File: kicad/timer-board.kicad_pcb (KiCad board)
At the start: 2 copper layers, 68.6 x 27.9 mm, 19 parts, among them J1 Conn_PWR, J2 Conn_Data, J3 JST Conn, SW1 SW_SPST, SW2 SW_SPDT, U1 NE555DR, U2 SN74HC00DR

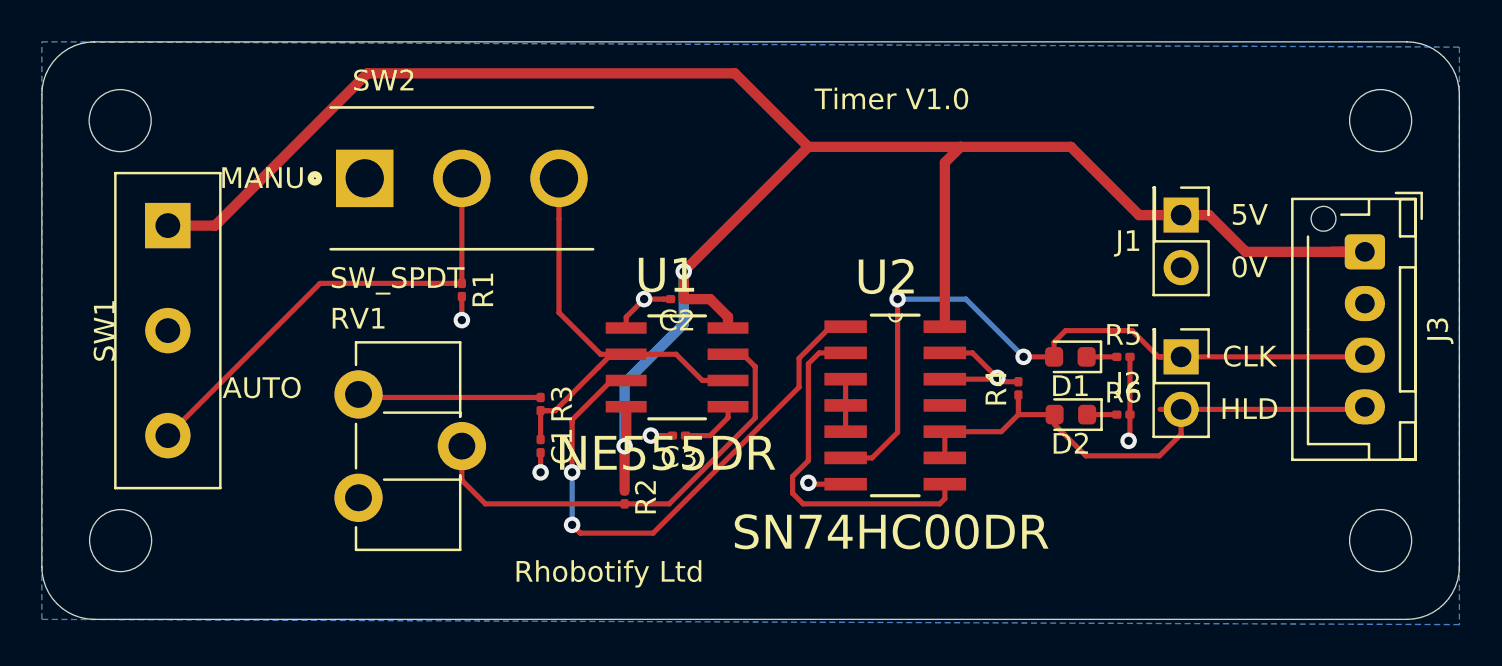
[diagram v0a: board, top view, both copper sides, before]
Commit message: Fix holes
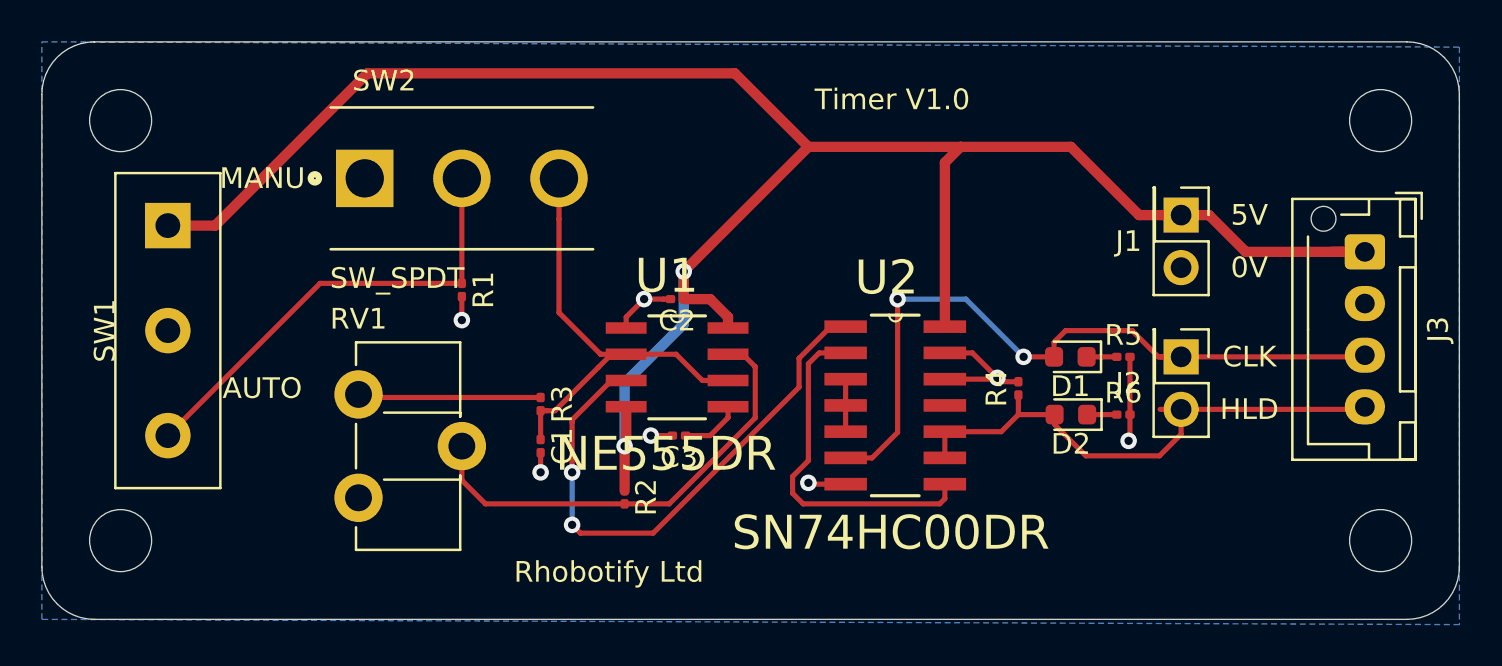
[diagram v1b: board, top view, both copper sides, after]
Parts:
- added REF**: MountingHole_3mm, MountingHole:MountingHole_3mm, F.Cu at (308.6, 105.4)
- added REF**: MountingHole_3mm, MountingHole:MountingHole_3mm, F.Cu at (308.6, 125.7)
- added REF**: MountingHole_3mm, MountingHole:MountingHole_3mm, F.Cu at (369.6, 125.7)
- added REF**: MountingHole_3mm, MountingHole:MountingHole_3mm, F.Cu at (369.6, 105.4)
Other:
- outline, holes or cut-outs redrawn
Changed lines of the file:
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@@
   (general
     (thickness 1.6)
-    (drawings 20)
+    (drawings 16)
     (tracks 140)
     (zones 0)
-    (modules 19)
+    (modules 23)
     (nets 15)
   )
@@
     (add_net "Net-(U2-Pad3)")
   )
+  (module MountingHole:MountingHole_3mm (layer F.Cu)
+    (at 308.61 105.41)
+    (descr "Mounting Hole 3mm, no annular")
+    (tags "mounting hole 3mm no annular")
+    (attr virtual)
+    (fp_text reference REF** (at 0 -4) (layer F.SilkS) hide
+      (effects (font (size 1 1) (thickness 0.15)))
+    )
+    (fp_text value MountingHole_3mm (at 0 4) (layer F.Fab)
+      (effects (font (size 1 1) (thickness 0.15)))
+    )
+    (fp_text user %R (at 0.3 0) (layer F.Fab)
+      (effects (font (size 1 1) (thickness 0.15)))
+    )
+    (fp_circle (center 0 0) (end 3 0) (layer Cmts.User) (width 0.15))
+    (fp_circle (center 0 0) (end 3.25 0) (layer F.CrtYd) (width 0.05))
+    (pad 1 np_thru_hole circle (at 0 0) (size 3 3) (drill 3) (layers *.Cu *.Mask))
+  )
+  (module MountingHole:MountingHole_3mm (layer F.Cu)
+    (at 308.61 125.73)
+    (descr "Mounting Hole 3mm, no annular")
+    (tags "mounting hole 3mm no annular")
+    (attr virtual)
+    (fp_text reference REF** (at 0 -4) (layer F.SilkS) hide
+      (effects (font (size 1 1) (thickness 0.15)))
+    )
+    (fp_text value MountingHole_3mm (at 0 4) (layer F.Fab)
+      (effects (font (size 1 1) (thickness 0.15)))
+    )
+    (fp_text user %R (at 0.3 0) (layer F.Fab)
+      (effects (font (size 1 1) (thickness 0.15)))
+    )
+    (fp_circle (center 0 0) (end 3 0) (layer Cmts.User) (width 0.15))
+    (fp_circle (center 0 0) (end 3.25 0) (layer F.CrtYd) (width 0.05))
+    (pad 1 np_thru_hole circle (at 0 0) (size 3 3) (drill 3) (layers *.Cu *.Mask))
+  )
+  (module MountingHole:MountingHole_3mm (layer F.Cu)
+    (at 369.57 125.73)
+    (descr "Mounting Hole 3mm, no annular")
+    (tags "mounting hole 3mm no annular")
+    (attr virtual)
+    (fp_text reference REF** (at 0 -4) (layer F.SilkS) hide
+      (effects (font (size 1 1) (thickness 0.15)))
+    )
+    (fp_text value MountingHole_3mm (at 0 4) (layer F.Fab)
+      (effects (font (size 1 1) (thickness 0.15)))
+    )
+    (fp_text user %R (at 0.3 0) (layer F.Fab)
+      (effects (font (size 1 1) (thickness 0.15)))
+    )
+    (fp_circle (center 0 0) (end 3 0) (layer Cmts.User) (width 0.15))
+    (fp_circle (center 0 0) (end 3.25 0) (layer F.CrtYd) (width 0.05))
+    (pad 1 np_thru_hole circle (at 0 0) (size 3 3) (drill 3) (layers *.Cu *.Mask))
+  )
+  (module MountingHole:MountingHole_3mm (layer F.Cu)
+    (at 369.57 105.41)
+    (descr "Mounting Hole 3mm, no annular")
+    (tags "mounting hole 3mm no annular")
+    (attr virtual)
+    (fp_text reference REF** (at 0 -4) (layer F.SilkS) hide
+      (effects (font (size 1 1) (thickness 0.15)))
+    )
+    (fp_text value MountingHole_3mm (at 0 4) (layer F.Fab)
+      (effects (font (size 1 1) (thickness 0.15)))
+    )
+    (fp_circle (center 0 0) (end 3.25 0) (layer F.CrtYd) (width 0.05))
+    (fp_circle (center 0 0) (end 3 0) (layer Cmts.User) (width 0.15))
+    (fp_text user %R (at 0.3 0) (layer F.Fab)
+      (effects (font (size 1 1) (thickness 0.15)))
+    )
+    (pad 1 np_thru_hole circle (at 0 0) (size 3 3) (drill 3) (layers *.Cu *.Mask))
+  )
   (module Connector_JST:JST_XH_B4B-XH-AM_1x04_P2.50mm_Vertical (layer F.Cu)
     (at 368.808 111.76 270)
@@
       (net 9 +5V))
   )
-  (gr_circle (center 369.57 105.41) (end 371.07 105.41) (layer Edge.Cuts) (width 0.05))
-  (gr_circle (center 369.57 125.73) (end 371.07 125.73) (layer Edge.Cuts) (width 0.05))
-  (gr_circle (center 308.61 125.73) (end 310.11 125.73) (layer Edge.Cuts) (width 0.05))
-  (gr_circle (center 308.588979 105.41) (end 310.088979 105.41) (layer Edge.Cuts) (width 0.05))
   (gr_arc (start 370.84 127) (end 370.84 129.54) (angle -90) (layer Edge.Cuts) (width 0.05))
   (gr_arc (start 307.34 127) (end 304.8 127) (angle -90) (layer Edge.Cuts) (width 0.05))

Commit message: Version 1.1
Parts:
- removed REF** (x4): MountingHole_3mm, MountingHole:MountingHole_3mm
- C1, C2, C3: footprint Capacitor_SMD:C_0201_0603Metric -> Capacitor_SMD:C_0603_1608Metric
- R1, R2, R3, R4, R5, R6: footprint Resistor_SMD:R_0201_0603Metric -> Resistor_SMD:R_0603_1608Metric
- moved R4 1.89 mm to (350.6, 119.6)
- moved D2 1.66 mm to (352.9, 119.5)
- moved D1 1.63 mm to (352.9, 116.8)
- moved C1 1.52 mm to (328.9, 122.7)
- moved R6 0.90 mm to (356.2, 119.5)
- moved R5 0.89 mm to (356.2, 116.8)
- moved R3 0.51 mm to (328.9, 119.6)
- moved R2 0.44 mm to (333.0, 123.2)
- moved C3 0.12 mm to (335.5, 120.7)
- moved C2 0.08 mm to (335.5, 114.0)
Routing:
- net GND: track 18.8 -> 23.7 mm, vias 7 -> 6
- net /Clk: track 36.5 -> 31.9 mm, vias 2 -> 0
- net /Hold: track 26.7 -> 23.4 mm
- net Net-(U1-Pad3): track 26.8 -> 29.6 mm
- net +5V: track 100.8 -> 98.6 mm
- net Net-(R2-Pad2): track 22.1 -> 23.9 mm
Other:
- board text added: "Timer V1.1"
- board text removed: "Timer V1.0"

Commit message: Update pot footprint
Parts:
- RV1: footprint Potentiometer_THT:Potentiometer_ACP_CA9-H5_Horizontal -> mine:6mm_trimmer
- moved RV1 1.45 mm to (318.8, 118.1)
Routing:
- net /Clk: track 31.9 -> 31.2 mm
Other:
- board text added: "Timer V1.2"
- board text removed: "Timer V1.1"
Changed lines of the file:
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@@
     (thickness 1.6)
     (drawings 16)
-    (tracks 136)
+    (tracks 134)
     (zones 0)
     (modules 19)
@@
     (add_net "Net-(U2-Pad3)")
   )
+  (module mine:6mm_trimmer (layer F.Cu)
+    (at 318.77 118.122)
+    (fp_text reference RV1 (at 4.3 -1.2) (layer F.SilkS)
+      (effects (font (size 1 1) (thickness 0.15)))
+    )
+    (fp_text value 1M (at 4.3 -2.2) (layer F.Fab)
+      (effects (font (size 1 1) (thickness 0.15)))
+    )
+    (fp_line (start 6.8 6) (end 6.3 6.5) (layer F.SilkS) (width 0.12))
+    (fp_line (start 6.3 0) (end 6.8 0.5) (layer F.SilkS) (width 0.12))
+    (fp_line (start 0 6.5) (end 0 0) (layer F.SilkS) (width 0.12))
+    (fp_line (start 6.3 6.5) (end 0 6.5) (layer F.SilkS) (width 0.12))
+    (fp_line (start 6.8 0.5) (end 6.8 6) (layer F.SilkS) (width 0.12))
+    (fp_line (start 0 0) (end 6.3 0) (layer F.SilkS) (width 0.12))
+    (pad 2 thru_hole circle (at 6.3 3.25) (size 2 2) (drill 1) (layers *.Cu *.Mask)
+      (net 6 "Net-(R2-Pad2)"))
+    (pad 3 thru_hole circle (at 1.4 5.75) (size 2 2) (drill 1) (layers *.Cu *.Mask))
+    (pad 1 thru_hole circle (at 1.4 0.75) (size 2 2) (drill 1) (layers *.Cu *.Mask)
+      (net 7 "Net-(R3-Pad1)"))
+  )
   (module Resistor_SMD:R_0603_1608Metric (layer F.Cu)
     (at 356.235 119.507)
@@
       (net 14 /Clk))
     (model ${KISYS3DMOD}/Connector_PinHeader_2.54mm.3dshapes/PinHeader_2x01_P2.54mm_Vertical.wrl
-      (at (xyz 0 0 0))
-      (scale (xyz 1 1 1))
-      (rotate (xyz 0 0 0))
-    )
-  )
-  (module Potentiometer_THT:Potentiometer_ACP_CA9-H5_Horizontal (layer F.Cu)
-    (at 320.12 118.658)
-    (descr "Potentiometer, horizontal, ACP CA9-H5, http://www.acptechnologies.com/wp-content/uploads/2017/05/02-ACP-CA9-CE9.pdf")
-    (tags "Potentiometer horizontal ACP CA9-H5")
-    (fp_text reference RV1 (at 0 -3.65) (layer F.SilkS)
-      (effects (font (size 1 1) (thickness 0.15)))
-    )
-    (fp_text value 1M (at 0 8.65) (layer F.Fab)
-      (effects (font (size 1 1) (thickness 0.15)))
-    )
-    (fp_line (start 4.8 -2.4) (end 4.8 7.4) (layer F.Fab) (width 0.1))
-    (fp_line (start 4.8 7.4) (end 0 7.4) (layer F.Fab) (width 0.1))
-    (fp_line (start 0 7.4) (end 0 -2.4) (layer F.Fab) (width 0.1))
-    (fp_line (start 0 -2.4) (end 4.8 -2.4) (layer F.Fab) (width 0.1))
-    (fp_line (start 0 1) (end 0 4) (layer F.Fab) (width 0.1))
-    (fp_line (start 0 4) (end 4.8 4) (layer F.Fab) (width 0.1))
-    (fp_line (start 4.8 4) (end 4.8 1) (layer F.Fab) (width 0.1))
-    (fp_line (start 4.8 1) (end 0 1) (layer F.Fab) (width 0.1))
-    (fp_line (start -0.121 -2.521) (end 4.92 -2.521) (layer F.SilkS) (width 0.12))
-    (fp_line (start -0.121 7.52) (end 4.92 7.52) (layer F.SilkS) (width 0.12))
-    (fp_line (start 4.92 -2.521) (end 4.92 1.075) (layer F.SilkS) (width 0.12))
-    (fp_line (start 4.92 3.925) (end 4.92 7.52) (layer F.SilkS) (width 0.12))
-    (fp_line (start -0.121 6.425) (end -0.121 7.52) (layer F.SilkS) (width 0.12))
-    (fp_line (start -0.121 -2.521) (end -0.121 -1.426) (layer F.SilkS) (width 0.12))
-    (fp_line (start -0.121 1.426) (end -0.121 3.575) (layer F.SilkS) (width 0.12))
-    (fp_line (start 1.237 0.88) (end 4.92 0.88) (layer F.SilkS) (width 0.12))
-    (fp_line (start 1.237 4.12) (end 4.92 4.12) (layer F.SilkS) (width 0.12))
-    (fp_line (start -0.121 1.426) (end -0.121 3.575) (layer F.SilkS) (width 0.12))
-    (fp_line (start 4.92 0.88) (end 4.92 1.075) (layer F.SilkS) (width 0.12))
-    (fp_line (start 4.92 3.925) (end 4.92 4.12) (layer F.SilkS) (width 0.12))
-    (fp_line (start -1.45 -2.7) (end -1.45 7.65) (layer F.CrtYd) (width 0.05))
-    (fp_line (start -1.45 7.65) (end 6.45 7.65) (layer F.CrtYd) (width 0.05))
-    (fp_line (start 6.45 7.65) (end 6.45 -2.7) (layer F.CrtYd) (width 0.05))
-    (fp_line (start 6.45 -2.7) (end -1.45 -2.7) (layer F.CrtYd) (width 0.05))
-    (fp_text user %R (at 2.4 2.5) (layer F.Fab)
-      (effects (font (size 1 1) (thickness 0.15)))
-    )
-    (pad 3 thru_hole circle (at 0 5) (size 2.34 2.34) (drill 1.3) (layers *.Cu *.Mask))
-    (pad 2 thru_hole circle (at 5 2.5) (size 2.34 2.34) (drill 1.3) (layers *.Cu *.Mask)
-      (net 6 "Net-(R2-Pad2)"))
-    (pad 1 thru_hole circle (at 0 0) (size 2.34 2.34) (drill 1.3) (layers *.Cu *.Mask)
-      (net 7 "Net-(R3-Pad1)"))
-    (model ${KISYS3DMOD}/Potentiometer_THT.3dshapes/Potentiometer_ACP_CA9-H5_Horizontal.wrl
       (at (xyz 0 0 0))
       (scale (xyz 1 1 1))
@@
     (effects (font (size 1 1) (thickness 0.15)))
   )
-  (gr_text "Timer V1.1" (at 345.948 104.394) (layer F.SilkS)
+  (gr_text "Timer V1.2" (at 345.948 104.394) (layer F.SilkS)
     (effects (font (size 1 1) (thickness 0.15)))
   )
@@
   (segment (start 337.9978 116.713) (end 338.709 116.713) (width 0.25) (layer F.Cu) (net 6))
   (segment (start 338.709 116.713) (end 339.598 117.602) (width 0.25) (layer F.Cu) (net 6))
-  (segment (start 320.268 118.806) (end 320.12 118.658) (width 0.25) (layer F.Cu) (net 7))
   (segment (start 328.93 118.806) (end 320.268 118.806) (width 0.25) (layer F.Cu) (net 7))
   (via (at 330.454 122.428) (size 0.8) (drill 0.4) (layers F.Cu B.Cu) (net 8))
@@
   (segment (start 336.3215 113.9698) (end 336.3215 112.2425) (width 0.5) (layer F.Cu) (net 9))
   (segment (start 336.3215 112.2425) (end 337.8708 110.6932) (width 0.5) (layer F.Cu) (net 9))
-  (via (at 332.994 120.3198) (size 0.8) (drill 0.4) (layers F.Cu B.Cu) (net 9) (status 1000000))
+  (via (at 332.994 120.3198) (size 0.8) (drill 0.4) (layers F.Cu B.Cu) (net 9))
   (segment (start 336.3214 116.9924) (end 332.994 120.3198) (width 0.5) (layer B.Cu) (net 9))
   (segment (start 336.3214 112.2426) (end 336.3214 116.9924) (width 0.5) (layer B.Cu) (net 9))
@@
   (segment (start 343.6874 120.46) (end 343.6874 119.19) (width 0.25) (layer F.Cu) (net 13))
   (segment (start 343.6874 117.92) (end 343.6874 119.19) (width 0.25) (layer F.Cu) (net 13))
-  (segment (start 343.6874 121.73) (end 344.4113 121.73) (width 0.25) (layer F.Cu) (net 14))
   (segment (start 359.918 115.74) (end 359.918 116.84) (width 0.25) (layer F.Cu) (net 14))
   (segment (start 359.748 115.57) (end 359.918 115.74) (width 0.25) (layer F.Cu) (net 14))
